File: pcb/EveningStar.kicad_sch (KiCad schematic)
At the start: 4 parts

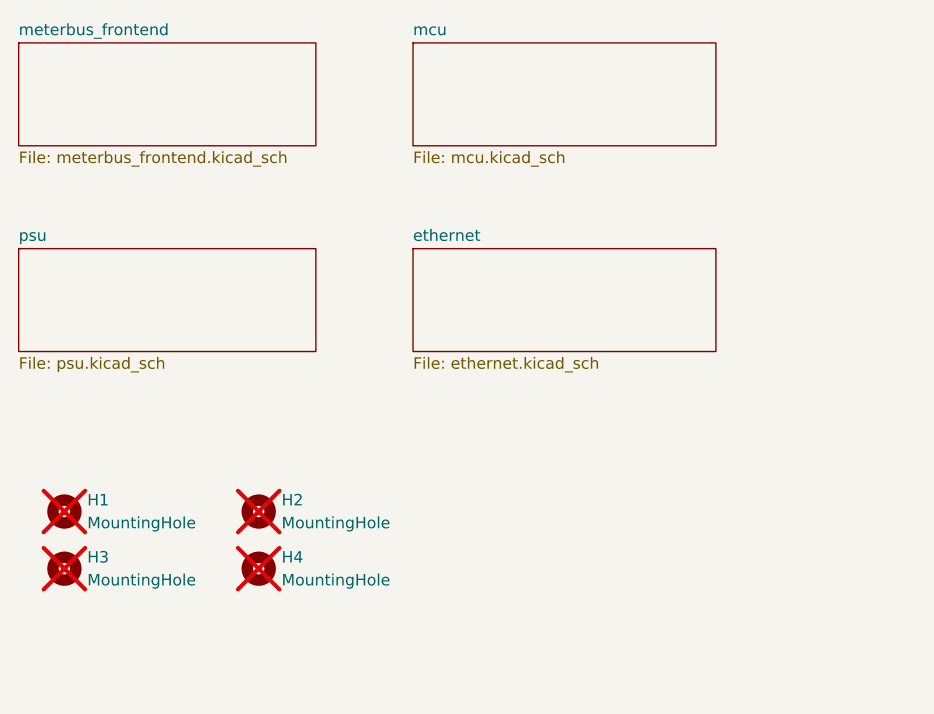
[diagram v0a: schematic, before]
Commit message: sch: clean up ethernet schematic
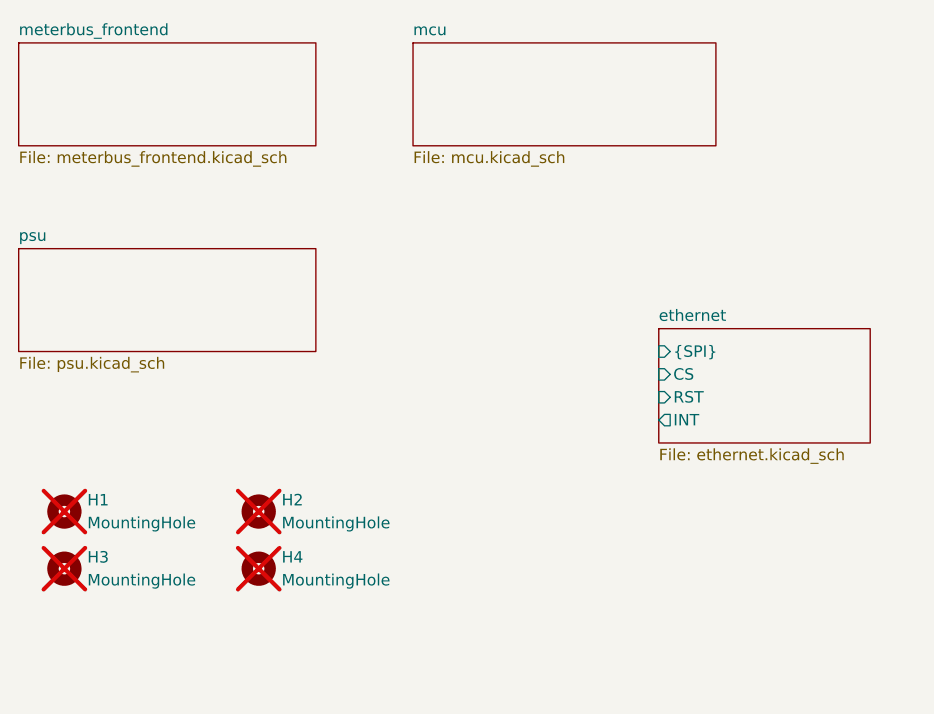
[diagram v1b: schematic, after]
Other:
- sheet ethernet ports: added CS, INT, RST, {SPI}; removed none
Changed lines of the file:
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@@
 	)
 	(sheet
-		(at 79.375 59.69)
-		(size 33.655 11.43)
+		(at 106.68 68.58)
+		(size 23.495 12.7)
 		(exclude_from_sim no)
 		(in_bom yes)
@@
 		)
 		(property "Sheetname" "ethernet"
-			(at 79.375 58.9784 0)
+			(at 106.68 67.8684 0)
 			(show_name no)
 			(do_not_autoplace no)
@@
 		)
 		(property "Sheetfile" "ethernet.kicad_sch"
-			(at 79.375 71.7046 0)
+			(at 106.68 81.8646 0)
 			(show_name no)
 			(do_not_autoplace no)
@@
 			)
 		)
+		(pin "RST" input
+			(at 106.68 76.2 180)
+			(effects
+				(font
+					(size 1.27 1.27)
+				)
+				(justify left)
+			)
+		)
+		(pin "INT" output
+			(at 106.68 78.74 180)
+			(effects
+				(font
+					(size 1.27 1.27)
+				)
+				(justify left)
+			)
+		)
+		(pin "{SPI}" input
+			(at 106.68 71.12 180)
+			(effects
+				(font
+					(size 1.27 1.27)
+				)
+				(justify left)
+			)
+		)
+		(pin "CS" input
+			(at 106.68 73.66 180)
+			(effects
+				(font
+					(size 1.27 1.27)
+				)
+				(justify left)
+			)
+		)

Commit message: sch: remove usb power and clean up mcu sheet
Fixes #15
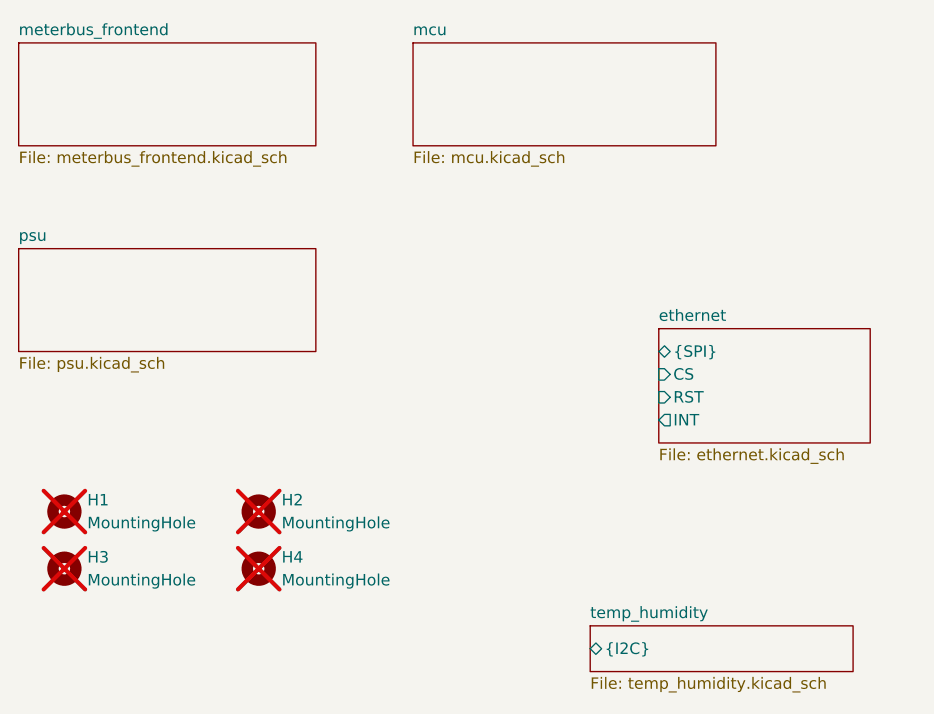
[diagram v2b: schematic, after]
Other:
- added sheet temp_humidity (temp_humidity.kicad_sch)
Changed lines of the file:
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@@
 			)
 		)
-		(pin "{SPI}" input
+		(pin "{SPI}" bidirectional
 			(at 106.68 71.12 180)
 			(effects
@@
 				)
 			)
+		)
+	)
+	(sheet
+		(at 99.06 101.6)
+		(size 29.21 5.08)
+		(exclude_from_sim no)
+		(in_bom yes)
+		(on_board yes)
+		(dnp no)
+		(fields_autoplaced yes)
+		(stroke
+			(width 0.1524)
+			(type solid)
+		)
+		(fill
+			(color 0 0 0 0)
+		)
+		(property "Sheetname" "temp_humidity"
+			(at 99.06 100.8884 0)
+			(show_name no)
+			(do_not_autoplace no)
+			(effects
+				(font
+					(size 1.27 1.27)
+				)
+				(justify left bottom)
+			)
+		)
+		(property "Sheetfile" "temp_humidity.kicad_sch"
+			(at 99.06 107.2646 0)
+			(show_name no)
+			(do_not_autoplace no)
+			(effects
+				(font
+					(size 1.27 1.27)
+				)
+				(justify left top)
+			)
+		)
+		(pin "{I2C}" bidirectional
+			(at 99.06 104.14 180)
+			(effects
+				(font
+					(size 1.27 1.27)
+				)
+				(justify left)
+			)
+		)
+		(instances
+			(project "EveningStar"
+				(path "/4c61f5a2-f8d4-462a-9bc3-d74437d30372"
+					(page "6")
+				)
+			)
